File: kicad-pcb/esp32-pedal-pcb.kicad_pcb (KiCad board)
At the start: 4 copper layers, 216 x 25 mm, 56 parts, among them J1 USB_C_Receptacle_USB2.0_14P, SW1 B2B-PH-K-S(LF)(SN), SW2 B2B-PH-K-S(LF)(SN), U1 MCP73871T-2CCI/ML, U2 TLV75733PDBV, U3 ESP32-S3-WROOM-1-N8, U4 TPD2EUSB30ADRTR, U6 TPS2553DBVR

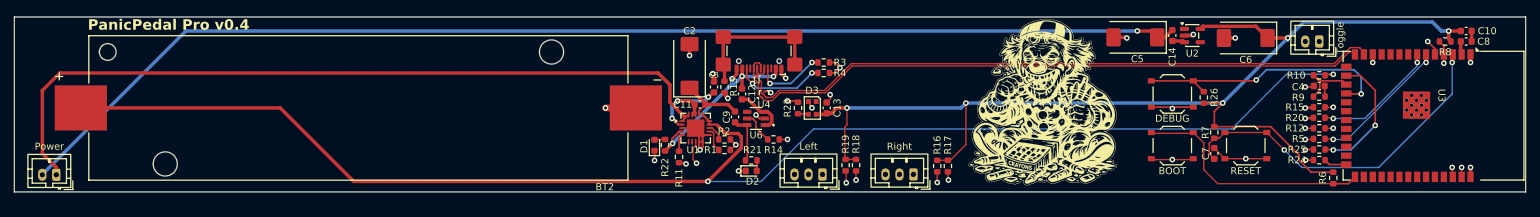
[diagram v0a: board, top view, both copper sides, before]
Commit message: Update board docs images and KiCad sources
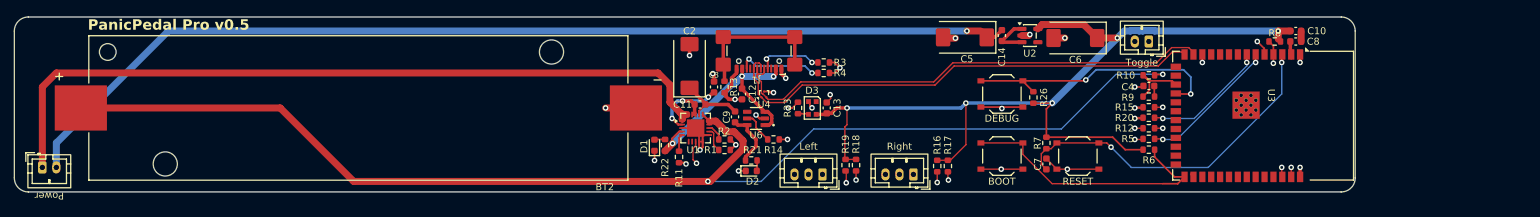
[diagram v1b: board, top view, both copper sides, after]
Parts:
- removed R24, R25: 100kΩ, Resistor_SMD:R_0603_1608Metric
- J1: value USB_C_Receptacle_USB2.0_14P -> USB4110-GF-A
- R23: value 220Ω -> 150Ω
- moved R6 26.7 mm to (195.6, 106.5), turned to 0 degrees
- moved BOOT1 24.4 mm to (174.6, 107.4)
- moved C10 24.4 mm to (216.6, 89.5)
- moved C14 24.4 mm to (174.6, 90.2)
- moved C6 24.4 mm to (185.1, 90.5)
- moved C8 24.4 mm to (216.6, 91.0)
- moved DEBUG1 24.4 mm to (174.6, 98.5)
- moved R10 24.4 mm to (195.6, 95.8)
- moved R12 24.4 mm to (195.6, 103.4)
- moved R15 24.4 mm to (195.6, 100.4)
- moved R20 24.4 mm to (195.6, 101.9)
- moved R26 24.4 mm to (179.1, 99.0)
- moved R8 24.4 mm to (213.6, 91.0)
- moved R9 24.4 mm to (195.6, 98.9)
- moved SW2 24.4 mm to (195.6, 91.0)
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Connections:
- C12 pad 1: /VBUS -> GND
- C12 pad 2: Net-(U6-EN) -> /VBUS
- U3 pad 16: /GPIO46 -> unconnected-(U3-GPIO46-Pad16)
- U3 pad 26: /GPIO45 -> unconnected-(U3-GPIO45-Pad26)
- U6 pad 1: Net-(U6-EN) -> /VBUS
- U6 pad 3: Net-(U6-EN) -> /VBUS
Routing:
- net /3V3: track 159.9 -> 129.0 mm
- net /GPIO8: track 96.9 -> 71.6 mm
- net /5V SWITCHED: track 170.8 -> 146.1 mm
- net Net-(Pedal2-Pin_3): track 68.6 -> 44.2 mm
- net Net-(Pedal2-Pin_1): track 64.5 -> 40.2 mm
- net Net-(Pedal1-Pin_1): track 76.0 -> 51.6 mm
- net Net-(Pedal1-Pin_3): track 80.3 -> 55.9 mm
- net /GPIO4/LBO: track 119.6 -> 95.2 mm
- net /D-: track 96.4 -> 72.3 mm
- net /D+: track 95.0 -> 70.8 mm
- net /VBAT: track 209.7 -> 185.7 mm
- net /GPIO46: track 18.7 -> 0.00 mm, vias 2 -> 0
- net /VBUS: track 26.7 -> 34.7 mm
- net Net-(U6-EN): track 7.32 -> 0.00 mm
- net Net-(U2-EN): track 1.80 -> 6.51 mm
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- removed copper zone on In2.Cu, net GND
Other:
- board size 216 x 25 mm -> 191.6 x 25 mm
- board text added: "PanicPedal Pro v0.5"
- board text added: "Schnicker Designs"
- board text added: "charles.daoust@gmail.com"
- board text added: "©2026"
- board text removed: "PanicPedal Pro v0.4"

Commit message: Unify debug messaging across all devices using shared DebugService
- Enhanced DebugService to support both EspNowTransport (transmitters) and ReceiverEspNowTransport (receiver) via function pointers
- Migrated receiver from DebugMonitor module to shared DebugService
- Added setDeviceType() to correctly tag debug messages with device type
- Fixed grace period timing issue when clearing MAC addresses (use currentTime instead of millis())
- Improved debug messages to distinguish between no transmitters loaded vs no replies
- All devices now use the same code for sending debug messages to debug monitor
- Message buffering works consistently across all device types
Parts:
- moved C2 13.6 mm to (126.0, 107.5), turned to 180 degrees
- moved R16 10.9 mm to (154.5, 108.6)
- moved R1 10.6 mm to (131.3, 95.0)
- moved R19 10.6 mm to (141.7, 108.7)
- moved R2 10.1 mm to (133.0, 96.6), turned to 180 degrees
- moved D1 9.03 mm to (133.0, 110.0)
- moved C12 8.89 mm to (131.7, 105.3)
- moved C11 8.14 mm to (137.0, 106.0)
- moved C3 7.91 mm to (129.0, 104.0), turned to 180 degrees
- moved R22 7.50 mm to (134.0, 106.0), turned to 0 degrees
- moved R13 6.26 mm to (132.0, 92.0)
- moved R21 6.18 mm to (136.0, 102.5), turned to -90 degrees
- moved R11 6.07 mm to (133.3, 103.7)
- moved R14 4.92 mm to (140.0, 100.5)
- moved R15 4.56 mm to (195.6, 105.0)
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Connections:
- R12 pad 2: /GPIO2 -> /GPIO6
- R15 pad 2: /GPIO1 -> /GPIO2
- R20 pad 1: /GPIO7 -> /GPIO1
- R5 pad 1: /GPIO6 -> /GPIO7
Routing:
- net /VBAT: track 185.7 -> 120.0 mm, vias 2 -> 3
- net GND: track 79.4 -> 49.5 mm, vias 25 -> 49
- net Net-(U1-CE): track 10.2 -> 28.8 mm, vias 0 -> 2
- net /5V: track 110.4 -> 98.1 mm, vias 0 -> 1
- net /GPIO8: track 71.6 -> 60.3 mm
- net /VBUS: track 34.7 -> 26.3 mm
- net /3V3: track 129.0 -> 136.0 mm, vias 5 -> 8
- net /GPIO4/LBO: track 95.2 -> 89.0 mm, vias 2 -> 0
- net /MCP IN: track 14.1 -> 20.0 mm
- net Net-(D2-A): track 1.52 -> 6.64 mm
- net Net-(Pedal2-Pin_3): track 44.2 -> 49.2 mm, vias 2 -> 0
- net /TPS OUT: track 8.10 -> 3.24 mm
- net /GPIO5: track 17.8 -> 21.2 mm
- net /GPIO9: track 10.2 -> 7.06 mm
- net /D+: track 70.8 -> 67.8 mm
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- added copper zone on F.Cu, net GND
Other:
- board size 191.6 x 25 mm -> 185.5 x 25 mm
- board text added: "PanicPedal Pro v0.7"
- board text removed: "PanicPedal Pro v0.5"
